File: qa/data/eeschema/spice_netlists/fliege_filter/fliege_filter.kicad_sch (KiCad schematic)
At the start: 12 parts, among them U1 LM358

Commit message: Sim: Remove inference from Reference and Value
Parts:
- C1: value C -> 10n; Sim_Device (none) -> C
- C2: renamed from C1; value C -> 10n; Sim_Device (none) -> C
- R1: value R -> 1M; Sim_Device (none) -> R
- R2: renamed from R1; value R -> 1M; Sim_Device (none) -> R
- R3, R4: renamed from R1; value R -> 15k; Sim_Device (none) -> R
- R5, R6: renamed from R1; value R -> 100k; Sim_Device (none) -> R
- V1: Sim_Device (none) -> V
- V4, V5: renamed from V1; value VDC -> 5; Sim_Device (none) -> V

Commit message: Sim: Rename Sim_* fields to Sim.*
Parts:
- C1, C2: Sim_Device C -> (none)
- R1, R2, R3, R4, R5, R6: Sim_Device R -> (none)
- U1: Sim_Device SUBCKT -> (none); Sim_Pins 8 4 3 2 1 5 6 7 -> (none)
- V1, V4, V5: Sim_Device V -> (none)
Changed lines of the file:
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@@
       (effects (font (size 1.27 1.27)) hide)
     )
-    (property "Sim_Device" "SUBCKT" (at 185.42 91.44 0)
-      (effects (font (size 1.27 1.27)) hide)
-    )
-    (property "Sim_Pins" "8 4 3 2 1 5 6 7" (at 154.94 91.44 0)
+    (property "Sim.Device" "SUBCKT" (at 185.42 91.44 0)
+      (effects (font (size 1.27 1.27)) hide)
+    )
+    (property "Sim.Pins" "8 4 3 2 1 5 6 7" (at 154.94 91.44 0)
       (effects (font (size 1.27 1.27)) hide)
     )
@@
       (effects (font (size 1.27 1.27)) hide)
     )
-    (property "Sim_Device" "R" (at 146.05 101.6 90)
+    (property "Sim.Device" "R" (at 146.05 101.6 90)
       (effects (font (size 1.27 1.27)) hide)
     )
@@
       (effects (font (size 1.27 1.27)) hide)
     )
-    (property "Sim_Device" "R" (at 196.85 133.35 0)
+    (property "Sim.Device" "R" (at 196.85 133.35 0)
       (effects (font (size 1.27 1.27)) hide)
     )
@@
       (effects (font (size 1.27 1.27)) hide)
     )
-    (property "Sim_Device" "V" (at 114.3 133.35 0)
+    (property "Sim.Device" "V" (at 114.3 133.35 0)
       (effects (font (size 1.27 1.27)) hide)
     )
@@
       (effects (font (size 1.27 1.27)) hide)
     )
-    (property "Sim_Device" "R" (at 184.15 101.6 90)
+    (property "Sim.Device" "R" (at 184.15 101.6 90)
       (effects (font (size 1.27 1.27)) hide)
     )
@@
       (effects (font (size 1.27 1.27)) hide)
     )
-    (property "Sim_Device" "SUBCKT" (at 185.42 149.86 0)
-      (effects (font (size 1.27 1.27)) hide)
-    )
-    (property "Sim_Pins" "8 4 3 2 1 5 6 7" (at 185.42 149.86 0)
+    (property "Sim.Device" "SUBCKT" (at 185.42 149.86 0)
+      (effects (font (size 1.27 1.27)) hide)
+    )
+    (property "Sim.Pins" "8 4 3 2 1 5 6 7" (at 185.42 149.86 0)
       (effects (font (size 1.27 1.27)) hide)
     )
@@
       (effects (font (size 1.27 1.27)) hide)
     )
-    (property "Sim_Device" "V" (at 114.3 95.25 0)
+    (property "Sim.Device" "V" (at 114.3 95.25 0)
       (effects (font (size 1.27 1.27)) hide)
     )
@@
       (effects (font (size 1.27 1.27)) hide)
     )
-    (property "Sim_Device" "C" (at 171.45 101.6 90)
+    (property "Sim.Device" "C" (at 171.45 101.6 90)
       (effects (font (size 1.27 1.27)) hide)
     )
@@
       (effects (font (size 1.27 1.27)) hide)
     )
-    (property "Sim_Device" "V" (at 114.3 120.65 0)
+    (property "Sim.Device" "V" (at 114.3 120.65 0)
       (effects (font (size 1.27 1.27)) hide)
     )
@@
       (effects (font (size 1.27 1.27)) hide)
     )
-    (property "Sim_Device" "SUBCKT" (at 185.42 91.44 0)
-      (effects (font (size 1.27 1.27)) hide)
-    )
-    (property "Sim_Pins" "8 4 3 2 1 5 6 7" (at 185.42 91.44 0)
+    (property "Sim.Device" "SUBCKT" (at 185.42 91.44 0)
+      (effects (font (size 1.27 1.27)) hide)
+    )
+    (property "Sim.Pins" "8 4 3 2 1 5 6 7" (at 185.42 91.44 0)
       (effects (font (size 1.27 1.27)) hide)
     )
@@
       (effects (font (size 1.27 1.27)) hide)
     )
-    (property "Sim_Device" "R" (at 158.75 95.25 0)
+    (property "Sim.Device" "R" (at 158.75 95.25 0)
       (effects (font (size 1.27 1.27)) hide)
     )
@@
       (effects (font (size 1.27 1.27)) hide)
     )
-    (property "Sim_Device" "C" (at 146.05 88.9 90)
+    (property "Sim.Device" "C" (at 146.05 88.9 90)
       (effects (font (size 1.27 1.27)) hide)
     )
@@
       (effects (font (size 1.27 1.27)) hide)
     )
-    (property "Sim_Device" "R" (at 196.85 107.95 0)
+    (property "Sim.Device" "R" (at 196.85 107.95 0)
       (effects (font (size 1.27 1.27)) hide)
     )
@@
       (effects (font (size 1.27 1.27)) hide)
     )
-    (property "Sim_Device" "R" (at 152.4 107.95 0)
-      (effects (font (size 1.27 1.27)) hide)
-    )
+    (property "Sim.Device" "R" (at 152.4 107.95 0)
+      (effects (font (size 1.27 1.27)) hide)
+    )

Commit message: Sim: Rename the missed Sim_* fields to Sim.*
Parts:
- U1: Sim_Library uopamp.lib.spice -> (none); Sim_Name uopamp_lvl2_2x -> (none)
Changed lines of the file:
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@@
       (effects (font (size 1.27 1.27)) hide)
     )
-    (property "Sim_Name" "uopamp_lvl2_2x" (at 185.42 91.44 0)
-      (effects (font (size 1.27 1.27)) hide)
-    )
-    (property "Sim_Library" "uopamp.lib.spice" (at 185.42 91.44 0)
+    (property "Sim.Name" "uopamp_lvl2_2x" (at 185.42 91.44 0)
+      (effects (font (size 1.27 1.27)) hide)
+    )
+    (property "Sim.Library" "uopamp.lib.spice" (at 185.42 91.44 0)
       (effects (font (size 1.27 1.27)) hide)
     )
@@
       (effects (font (size 1.27 1.27)) hide)
     )
-    (property "Sim_Name" "uopamp_lvl2_2x" (at 185.42 149.86 0)
-      (effects (font (size 1.27 1.27)) hide)
-    )
-    (property "Sim_Library" "uopamp.lib.spice" (at 185.42 149.86 0)
+    (property "Sim.Name" "uopamp_lvl2_2x" (at 185.42 149.86 0)
+      (effects (font (size 1.27 1.27)) hide)
+    )
+    (property "Sim.Library" "uopamp.lib.spice" (at 185.42 149.86 0)
       (effects (font (size 1.27 1.27)) hide)
     )
@@
       (effects (font (size 1.27 1.27)) hide)
     )
-    (property "Sim_Name" "uopamp_lvl2_2x" (at 185.42 91.44 0)
-      (effects (font (size 1.27 1.27)) hide)
-    )
-    (property "Sim_Library" "uopamp.lib.spice" (at 185.42 91.44 0)
-      (effects (font (size 1.27 1.27)) hide)
-    )
+    (property "Sim.Name" "uopamp_lvl2_2x" (at 185.42 91.44 0)
+      (effects (font (size 1.27 1.27)) hide)
+    )
+    (property "Sim.Library" "uopamp.lib.spice" (at 185.42 91.44 0)
+      (effects (font (size 1.27 1.27)) hide)
+    )

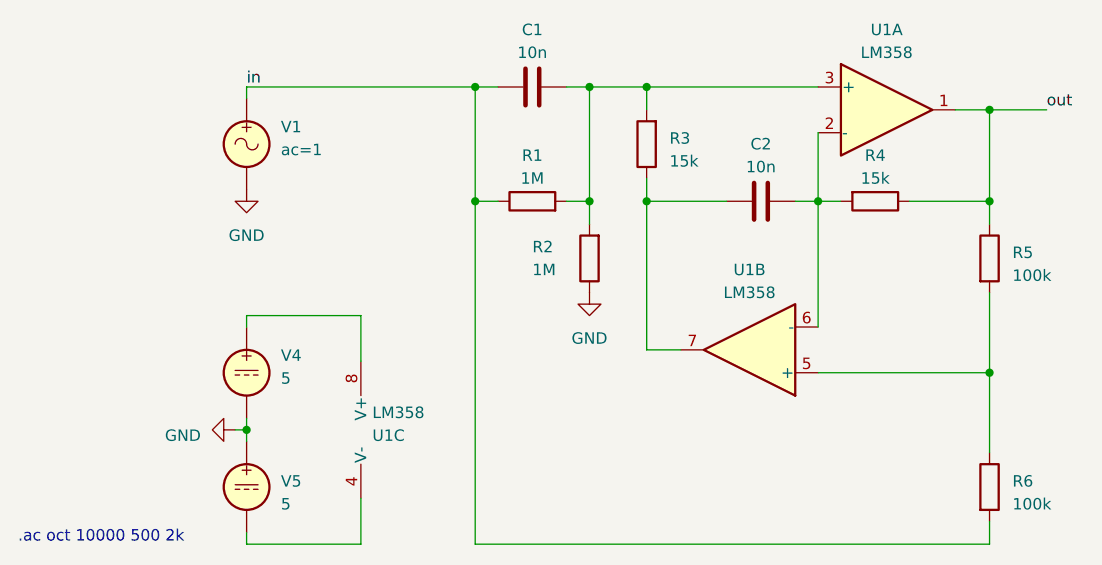
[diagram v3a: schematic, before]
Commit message: Sim QA: Fix QA errors
Let's not allow units in fields for now. (is 1m one meter or one milli?)
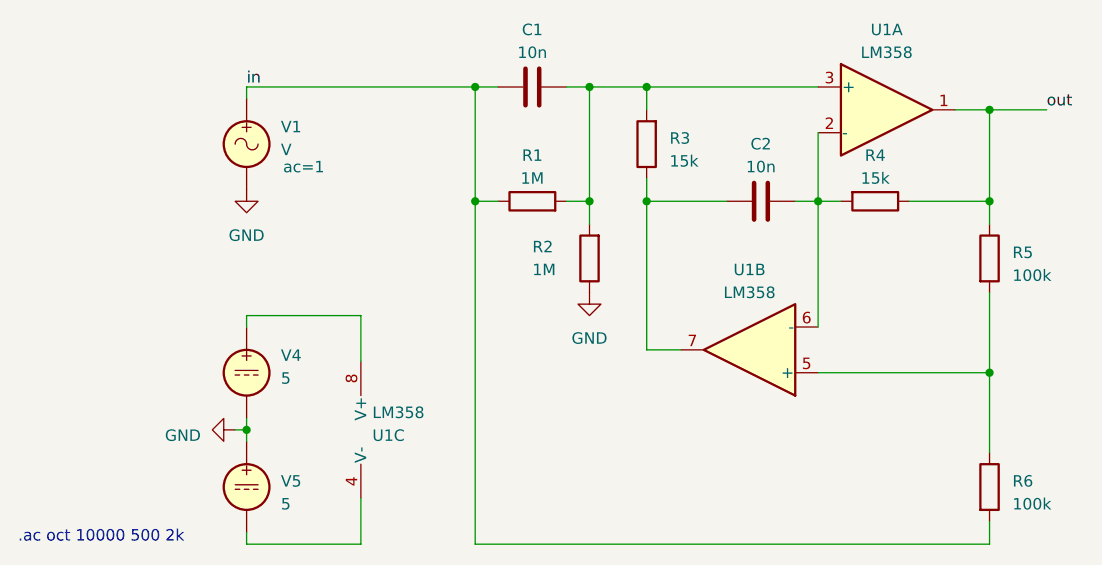
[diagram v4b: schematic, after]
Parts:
- V1: value ac=1 -> V
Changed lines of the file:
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@@
   )
   (symbol (lib_id "Simulation_SPICE:VSIN") (at 114.3 95.25 0) (unit 1)
-    (in_bom yes) (on_board yes) (dnp no) (fields_autoplaced)
+    (in_bom yes) (on_board yes) (dnp no)
     (property "Reference" "V1" (at 118.11 93.345 0)
       (effects (font (size 1.27 1.27)) (justify left))
     )
-    (property "Value" "ac=1" (at 118.11 95.885 0)
+    (property "Value" "V" (at 118.11 95.885 0)
       (effects (font (size 1.27 1.27)) (justify left))
     )
@@
       (effects (font (size 1.27 1.27)) hide)
     )
+    (property "Sim.Params" "ac=1" (at 120.65 97.79 0)
+      (effects (font (size 1.27 1.27)))
+    )
     (pin "1")
     (pin "2")
@@
       (project "fliege_filter"
         (path "/1bb7f68e-09b1-4448-8403-97b70f8d3680"
-          (reference "V1") (unit 1) (value "ac=1") (footprint "")
+          (reference "V1") (unit 1) (value "V") (footprint "")
         )
       )
